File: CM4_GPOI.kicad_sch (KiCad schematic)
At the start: 26 parts, among them J4 Conn_02x04_Odd_Even, J5 61900419521, M2 CM4-GPIO, U11 EMC2301, U5 74LVC1G07SE-7, U9 SLB9672XU20FW1612XTMA1

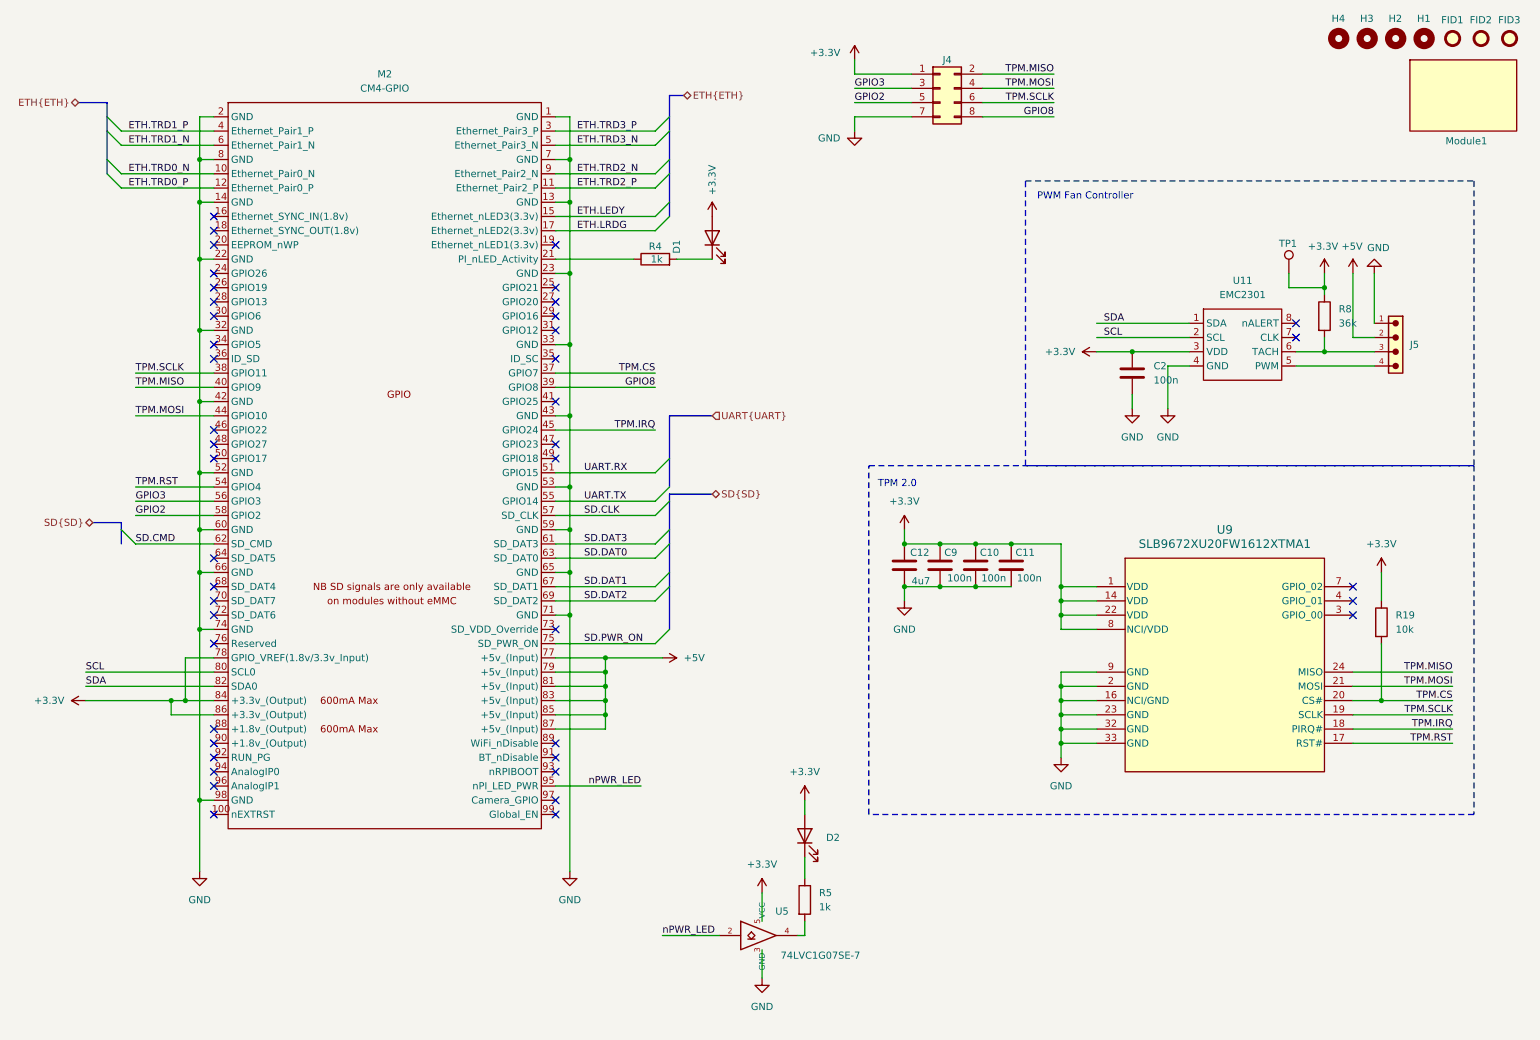
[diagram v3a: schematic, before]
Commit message: feat: use hardware components
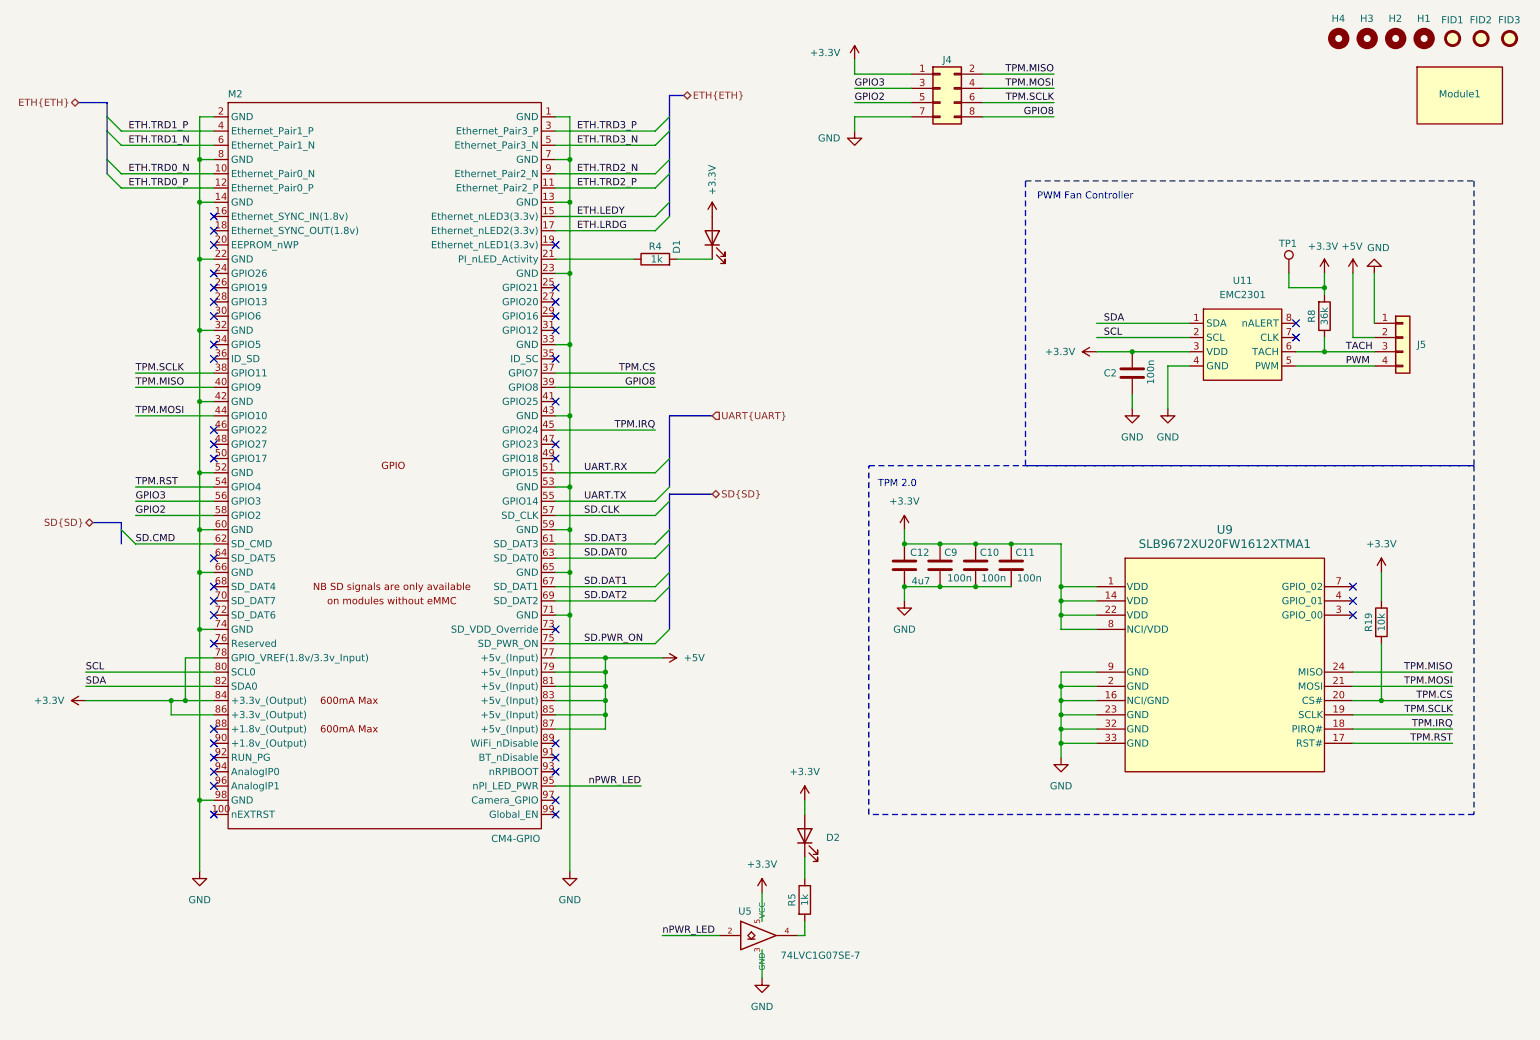
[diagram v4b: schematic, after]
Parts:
- C10, C11, C2, C9: footprint HomeLabIO:C_0402_1005Metric -> Hardware Components:C_0402_1005Metric; symbol HomeLabIO:C -> Hardware Components:C_100n_0402_16V
- C12: footprint HomeLabIO:C_0402_1005Metric -> Hardware Components:C_0402_1005Metric; symbol HomeLabIO:C -> Hardware Components:C_4u7_0402_16V
- D1: footprint LED_SMD:LED_0603_1608Metric -> Hardware Components:LED_0603_1608Metric; symbol HomeLabIO:LED -> Hardware Components:LED_G_0603_LTST-C191KGKT
- D2: footprint LED_SMD:LED_0603_1608Metric -> Hardware Components:LED_0603_1608Metric; symbol HomeLabIO:LED -> Hardware Components:LED_R_0603_LTST-C191KRKT
- J4: footprint Connector_PinHeader_2.54mm:PinHeader_2x04_P2.54mm_Vertical -> Hardware Components:Conn_PinHeader_2x04_P2.54mm_Vertical; symbol Connector_Generic:Conn_02x04_Odd_Even -> Hardware Components:Conn_PinHeader_2x04_P2.54mm_Vertical
- J5: footprint HomeLabIO:TE_640455-4 -> Hardware Components:Conn_PinHeader_1x04_P2.54mm_Horizontal_Latch; symbol HomeLabIO:640455-4 -> Hardware Components:Conn_PinHeader_1x04_P2.54mm_Horizontal_Latch
- M2: footprint HomeLabIO:HIROSE_DF40C-100DS-0.4V_51_ -> Hardware Components:Conn_Socket_HIROSE_DF40_2x50_DF40C-100DS-0.4V; symbol HomeLabIO:CM4-GPIO -> Hardware Components:Compute-Module-4_GPIO
- Module1: footprint HomeLabIO:Raspberry-Pi-4-Compute-Module -> Hardware Components:Compute-Module-4-H1; symbol HomeLabIO:ComputeModule4-CM4 -> Hardware Components:Compute-Module-4_H1; MPN (none) -> SC0294; Manufacturer Hirose -> Rapberry Pi
- R19: footprint HomeLabIO:R_0402_1005Metric -> Hardware Components:R_0402_1005Metric; symbol HomeLabIO:R -> Hardware Components:R_10k_0402_50V
- R4, R5: footprint HomeLabIO:R_0402_1005Metric -> Hardware Components:R_0402_1005Metric; symbol HomeLabIO:R -> Hardware Components:R_1k_0402_75V
- R8: footprint HomeLabIO:R_0402_1005Metric -> Hardware Components:R_0402_1005Metric; symbol HomeLabIO:R -> Hardware Components:R_36k_0402_50V
- U11: footprint HomeLabIO:MSOP8_MC_MCH -> Hardware Components:MSOP8_MC_MCH; symbol HomeLabIO:EMC2301 -> Hardware Components:Driver_EMC2301
- U5: footprint Package_TO_SOT_SMD:SOT-353_SC-70-5 -> Hardware Components:SOT-353_SC-70-5; symbol HomeLabIO:74LVC1G07SE-7 -> Hardware Components:74LVC1G07SE-7
- U9: footprint HomeLabIO:PG-UQFN-32-1_INF -> Hardware Components:UQFN-32-1; symbol HomeLabIO:SLB9672XU20FW1610XTMA1 -> Hardware Components:SLB9672XU20FW1610XTMA1
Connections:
- net TACH: now reaches J5.3 (Pin_3), R8.2, U11.6 (TACH)
- net PWM: now reaches J5.4 (Pin_4), U11.5 (PWM)
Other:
- moved on the sheet: Module1

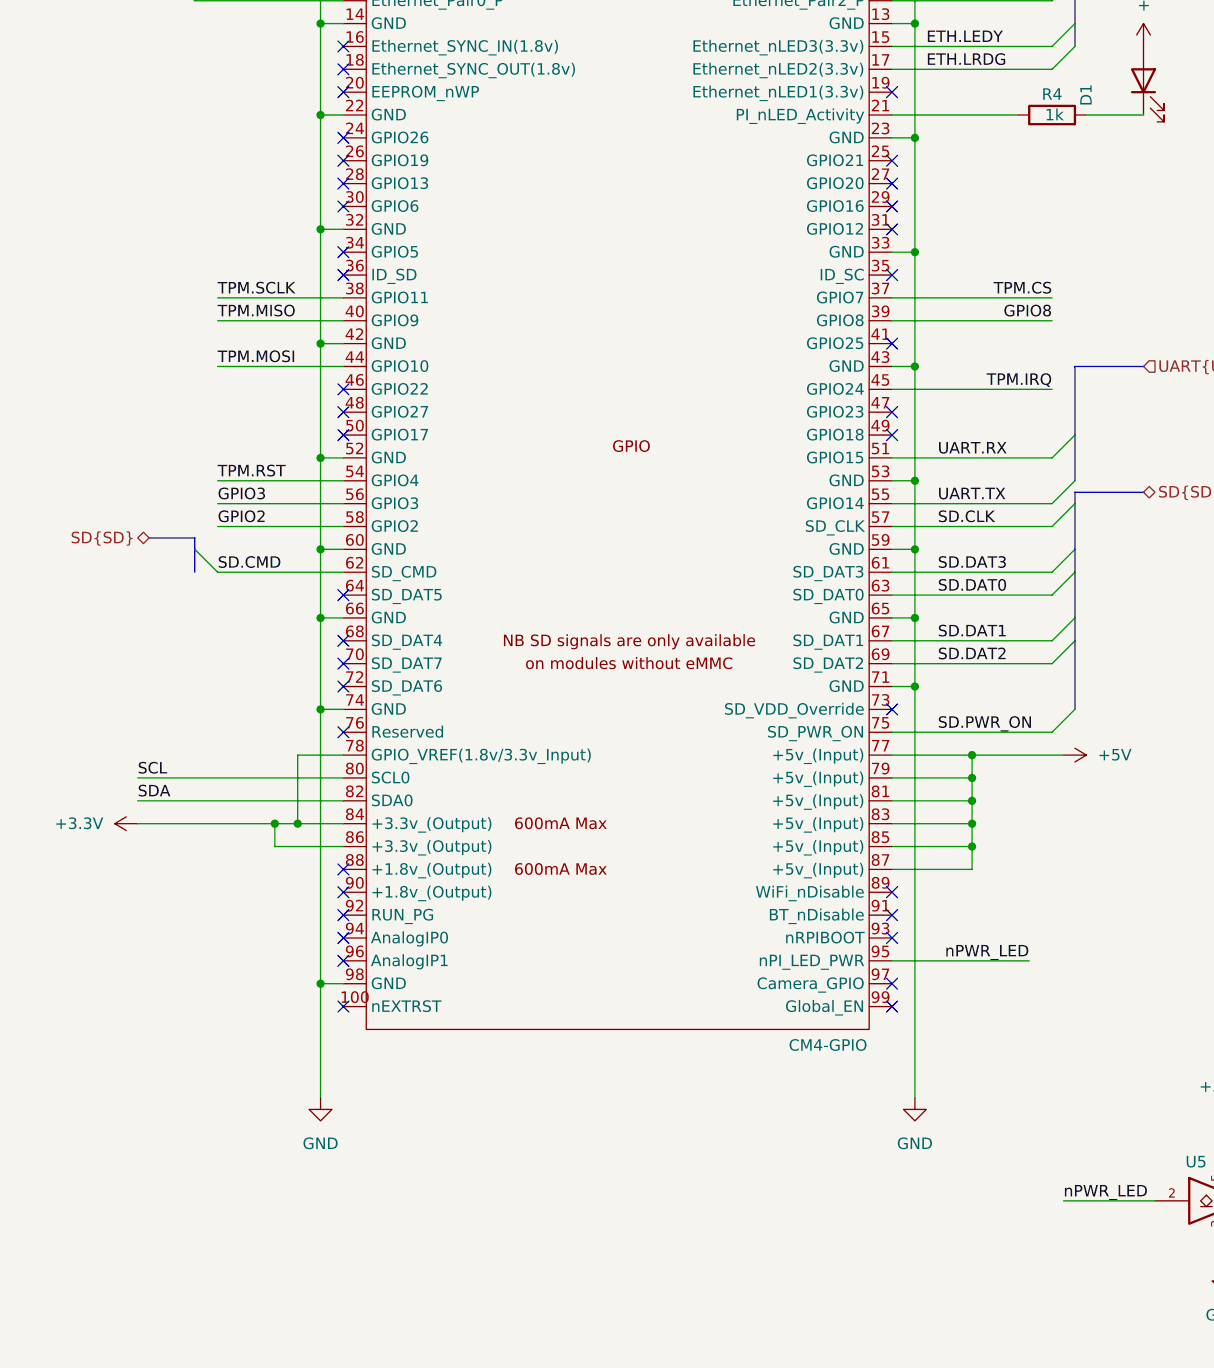
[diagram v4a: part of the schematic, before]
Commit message: wip: add button
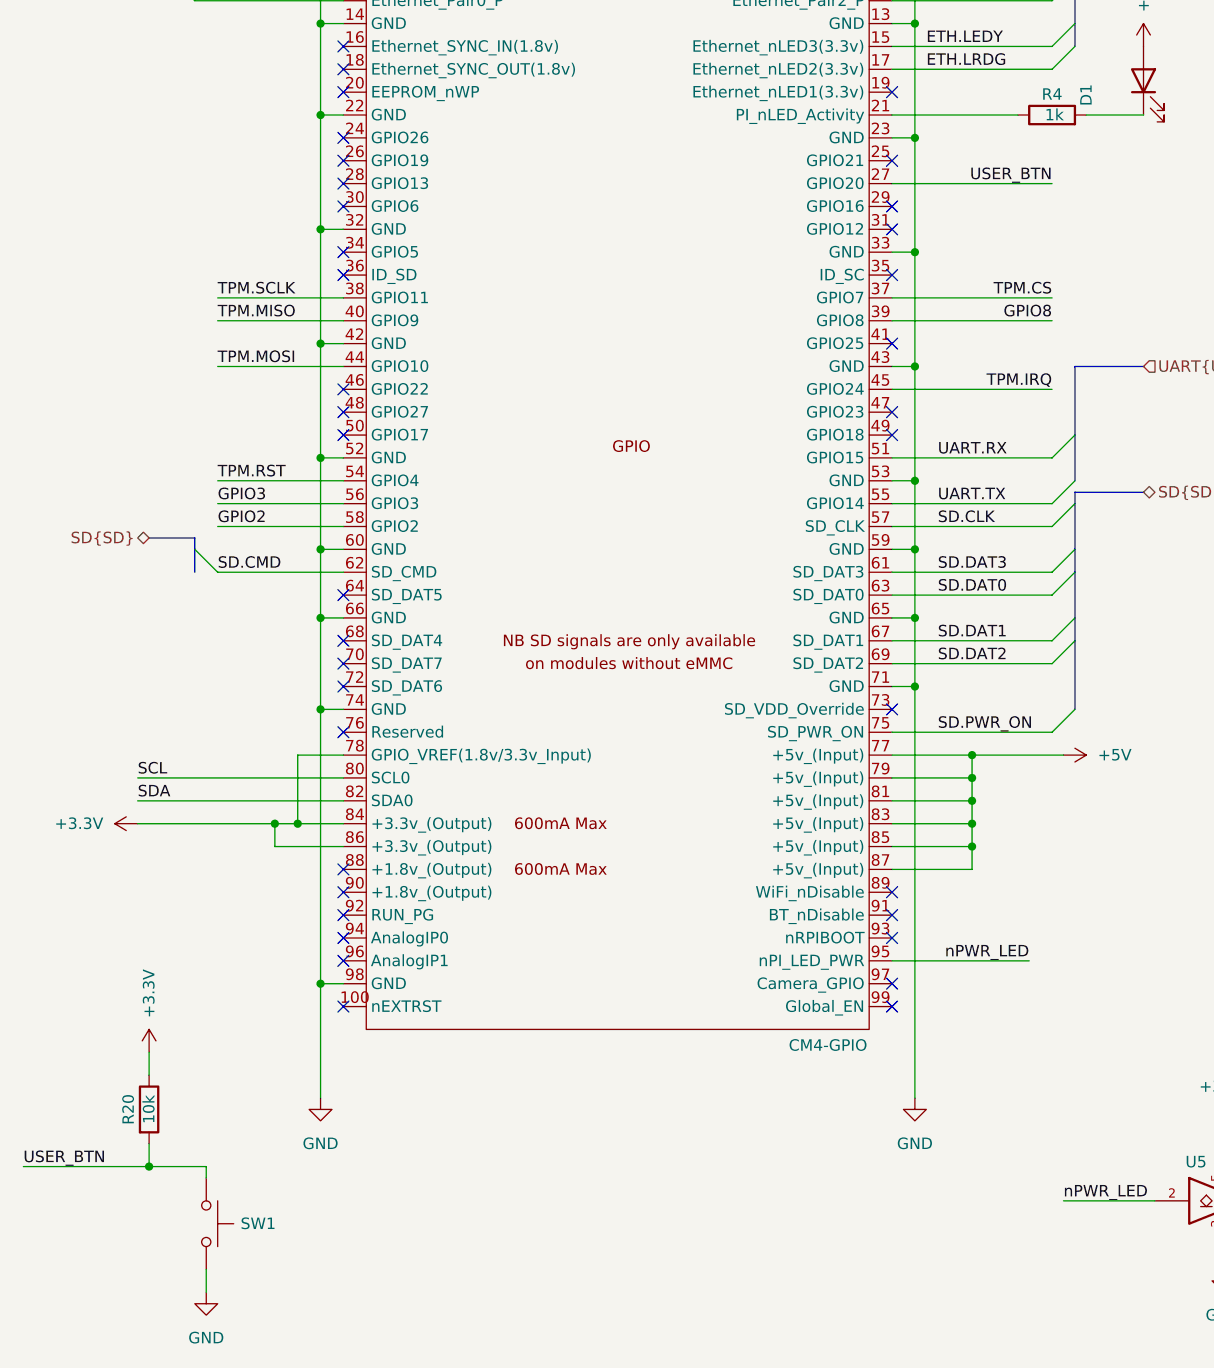
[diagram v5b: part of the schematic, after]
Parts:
- added R20: 10k, Hardware Components:R_0402_1005Metric, symbol Hardware Components:R_10k_0402_50V
- added SW1: SW_Push, Button_Switch_SMD:Panasonic_EVQPUL_EVQPUC, symbol Switch:SW_Push
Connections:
- net +3.3V: now also R20.1
- net GND: now also SW1.2
- net USER_BTN: now reaches M2.27 (GPIO20)
- net USER_BTN: now also R20.2, SW1.1
- no-connect marks 43 -> 42

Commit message: feat: finish front switch
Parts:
- SW1: footprint Button_Switch_SMD:Panasonic_EVQPUL_EVQPUC -> Hardware Components:SW_Panasonic_EVQPUC; symbol Switch:SW_Push -> Hardware Components:SW_Panasonic_EVQPUC02K
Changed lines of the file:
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@@
 	)
 	(symbol
-		(lib_id "Switch:SW_Push")
+		(lib_id "Hardware Components:SW_Panasonic_EVQPUC02K")
 		(at 35.56 181.61 270)
 		(unit 1)
@@
 			)
 		)
-		(property "Footprint" "Button_Switch_SMD:Panasonic_EVQPUL_EVQPUC"
+		(property "Footprint" "Hardware Components:SW_Panasonic_EVQPUC"
 			(at 40.64 181.61 0)
 			(effects
